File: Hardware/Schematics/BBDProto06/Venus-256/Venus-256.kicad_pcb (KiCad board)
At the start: 4 copper layers, 172.7 x 109.2 mm, 231 parts, among them J201 RaspberryPi header, J301 ARM JTAG, U1001 AD7616, U101 TPS22993, U401 AD7616, U501 ATSAME70Q21A-AN, U601 AD7616, U701 AD7616, U801 AD7616, U901 ATSAME70Q21A-AN

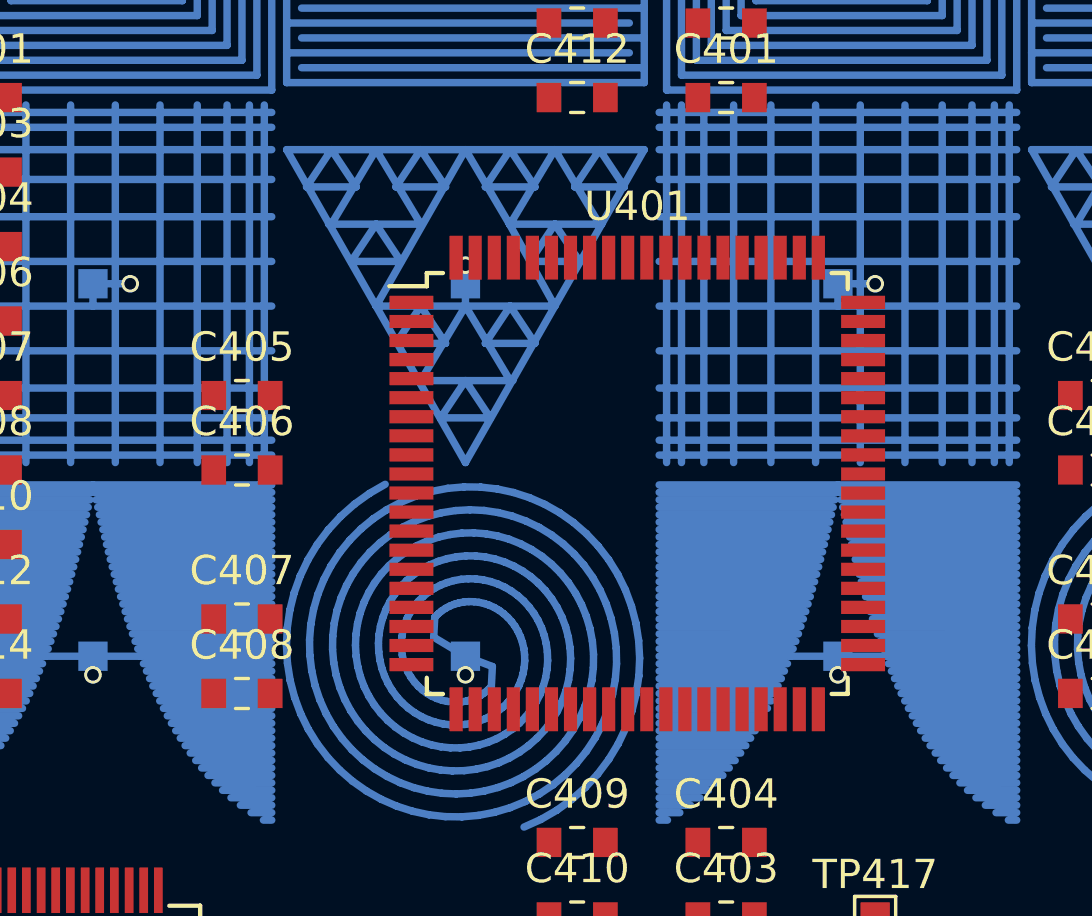
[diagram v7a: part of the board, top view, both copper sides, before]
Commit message: Moved the ADC to fit the 0.65 grid (its own pitch)
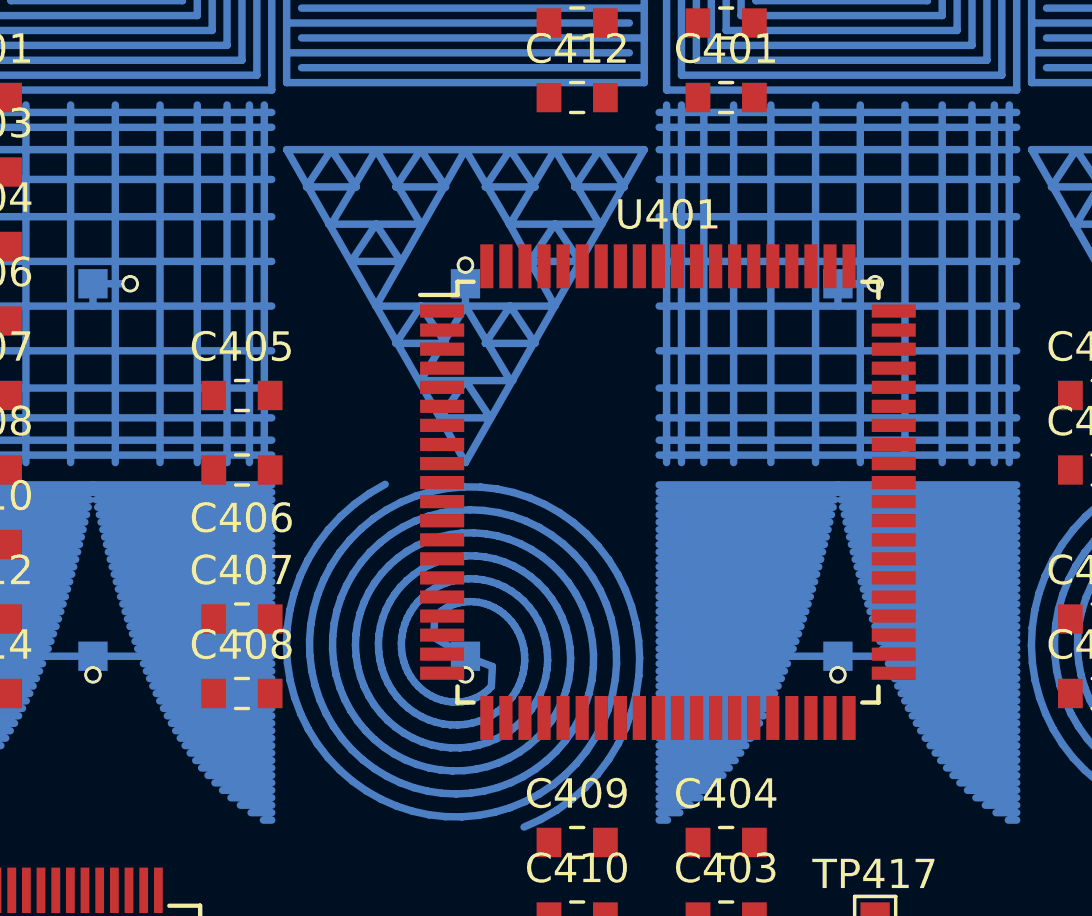
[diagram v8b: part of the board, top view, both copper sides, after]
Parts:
- moved U401 1.09 mm to (147.9, 46.5)
- turned C406 to 180 degrees
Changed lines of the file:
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@@
     (thickness 1.6)
     (drawings 249)
-    (tracks 9444)
+    (tracks 9445)
     (zones 0)
     (modules 231)
@@
   )
   (module Capacitor_SMD:C_0603_1608Metric_Pad0.84x1.00mm_HandSolder (layer F.Cu)
-    (at 133.35 45.72)
+    (at 133.35 45.72 180)
     (descr "Capacitor SMD 0603 (1608 Metric), square (rectangular) end terminal, IPC_7351 nominal with elongated pad for handsoldering. (Body size source: http://www.tortai-tech.com/upload/download/2011102023233369053.pdf), generated with kicad-footprint-generator")
     (tags "capacitor handsolder")
     (attr smd)
-    (fp_text reference C406 (at 0 -1.65) (layer F.SilkS)
+    (fp_text reference C406 (at 0 -1.65 180) (layer F.SilkS)
       (effects (font (size 1 1) (thickness 0.15)))
     )
-    (fp_text value 0.1uF (at 0 1.65) (layer F.Fab)
+    (fp_text value 0.1uF (at 0 1.65 180) (layer F.Fab)
       (effects (font (size 1 1) (thickness 0.15)))
     )
-    (fp_text user %R (at 0 0) (layer F.Fab)
+    (fp_text user %R (at 0 0 180) (layer F.Fab)
       (effects (font (size 0.5 0.5) (thickness 0.08)))
     )
@@
     (fp_line (start -0.8 -0.4) (end 0.8 -0.4) (layer F.Fab) (width 0.1))
     (fp_line (start -0.8 0.4) (end -0.8 -0.4) (layer F.Fab) (width 0.1))
-    (pad 2 smd rect (at 0.9625 0) (size 0.845 1) (layers F.Cu F.Paste F.Mask)
+    (pad 2 smd rect (at 0.9625 0 180) (size 0.845 1) (layers F.Cu F.Paste F.Mask)
       (net 1 GND))
-    (pad 1 smd rect (at -0.9625 0) (size 0.845 1) (layers F.Cu F.Paste F.Mask)
+    (pad 1 smd rect (at -0.9625 0 180) (size 0.845 1) (layers F.Cu F.Paste F.Mask)
       (net 2 /RaspberryPiGPIOHeader/DC_POWER_5V0))
     (model ${KISYS3DMOD}/Capacitor_SMD.3dshapes/C_0603_1608Metric.wrl
@@
   )
   (module Package_QFP:LQFP-80_14x14mm_P0.65mm (layer F.Cu)
-    (at 146.8275 46.18)
+    (at 147.875 46.475)
     (descr "80-Lead Quad Flatpack, 14x14x1.6mm Body (http://www.analog.com/media/en/technical-documentation/data-sheets/AD9852.pdf)")
     (tags "QFP 0.65")
@@
   (via blind (at 140.97 27.305) (size 0.6) (drill 0.4) (layers In2.Cu B.Cu) (net 43))
   (segment (start 140.97 26.67) (end 140.97 27.305) (width 0.254) (layer B.Cu) (net 43))
+  (segment (start 140.97 27.305) (end 140.97 27.37) (width 0.254) (layer In2.Cu) (net 43))
   (segment (start 128.27 27.686) (end 128.27 26.67) (width 0.254) (layer B.Cu) (net 44))
   (segment (start 126.492 28.702) (end 126.492 25.4) (width 0.254) (layer B.Cu) (net 44))
